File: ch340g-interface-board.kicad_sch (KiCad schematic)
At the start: 10 parts, among them J1 61729-1011BLF, J2 Conn_01x02_Pin, J3 Conn_01x06_Pin, U1 CH340G, Y1 12Mhz

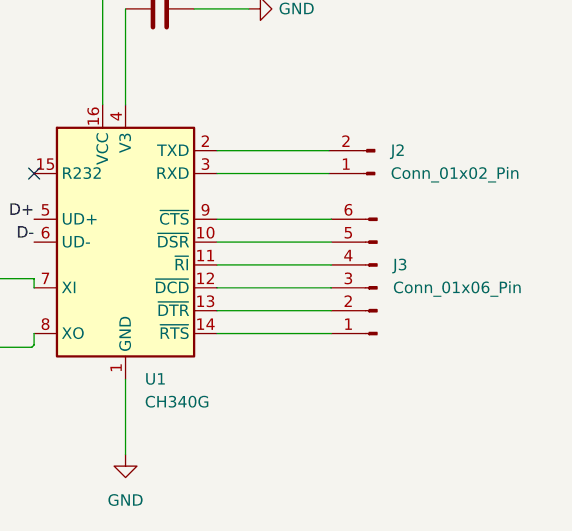
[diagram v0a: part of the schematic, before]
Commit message: documentation: board updates
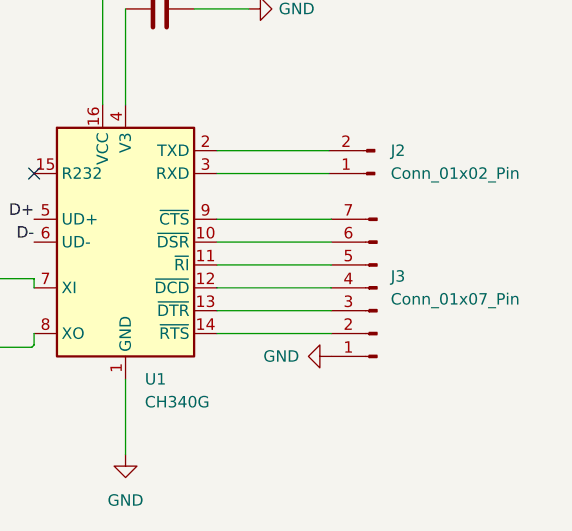
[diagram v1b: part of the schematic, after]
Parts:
- removed J3: Conn_01x06_Pin, Connector_PinHeader_1.00mm:PinHeader_1x06_P1.00mm_Vertical, symbol Connector:Conn_01x06_Pin
- added J3: Conn_01x07_Pin, Connector_PinHeader_1.00mm:PinHeader_1x07_P1.00mm_Vertical, symbol Connector:Conn_01x07_Pin
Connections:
- net GND: now also J3.1 (Pin_1)
- net at U1.10 (~{DSR}): now also J3.6 (Pin_6)
- net at U1.11 (~{RI}): now also J3.5 (Pin_5)
- net at U1.12 (~{DCD}): now also J3.4 (Pin_4)
- net at U1.13 (~{DTR}): now also J3.3 (Pin_3)
- net at U1.14 (~{RTS}): now also J3.2 (Pin_2)
- net at U1.9 (~{CTS}): now also J3.7 (Pin_7)
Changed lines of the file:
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@@
-	)
-	(symbol
-		(lib_id "Connector:Conn_01x06_Pin")
-		(at 136.906 63.5 180)
-		(unit 1)
-		(exclude_from_sim no)
-		(in_bom yes)
-		(on_board yes)
-		(dnp no)
-		(fields_autoplaced yes)
-		(property "Reference" "J3"
-			(at 138.684 60.9599 0)
-			(effects
-				(font
-					(size 1.27 1.27)
-				)
-				(justify right)
-			)
-		)
-		(property "Value" "Conn_01x06_Pin"
-			(at 138.684 63.4999 0)
-			(effects
-				(font
-					(size 1.27 1.27)
-				)
-				(justify right)
-			)
-		)
-		(property "Footprint" "Connector_PinHeader_1.00mm:PinHeader_1x06_P1.00mm_Vertical"
-			(at 136.906 63.5 0)
-			(effects
-				(font
-					(size 1.27 1.27)
-				)
-				(hide yes)
-			)
-		)
-		(property "Datasheet" "~"
-			(at 136.906 63.5 0)
-			(effects
-				(font
-					(size 1.27 1.27)
-				)
-				(hide yes)
-			)
-		)
-		(property "Description" "Generic connector, single row, 01x06, script generated"
-			(at 136.906 63.5 0)
-			(effects
-				(font
-					(size 1.27 1.27)
-				)
-				(hide yes)
-			)
-		)
-		(pin "4"
-		)
-		(pin "5"
-		)
-		(pin "6"
-		)
-		(pin "1"
-		)
-		(pin "2"
-		)
-		(pin "3"
-		)
-		(instances
-			(project ""
-				(path "/1242ce71-0b74-4298-a9a8-725f79ae9887"
-					(reference "J3")
-					(unit 1)
-				)
-			)
-		)
 	)
 	(symbol
@@
 	)
 	(symbol
+		(lib_id "Connector:Conn_01x07_Pin")
+		(at 136.906 63.5 180)
+		(unit 1)
+		(exclude_from_sim no)
+		(in_bom yes)
+		(on_board yes)
+		(dnp no)
+		(fields_autoplaced yes)
+		(property "Reference" "J3"
+			(at 138.43 62.2299 0)
+			(effects
+				(font
+					(size 1.27 1.27)
+				)
+				(justify right)
+			)
+		)
+		(property "Value" "Conn_01x07_Pin"
+			(at 138.43 64.7699 0)
+			(effects
+				(font
+					(size 1.27 1.27)
+				)
+				(justify right)
+			)
+		)
+		(property "Footprint" "Connector_PinHeader_1.00mm:PinHeader_1x07_P1.00mm_Vertical"
+			(at 136.906 63.5 0)
+			(effects
+				(font
+					(size 1.27 1.27)
+				)
+				(hide yes)
+			)
+		)
+		(property "Datasheet" "~"
+			(at 136.906 63.5 0)
+			(effects
+				(font
+					(size 1.27 1.27)
+				)
+				(hide yes)
+			)
+		)
+		(property "Description" "Generic connector, single row, 01x07, script generated"
+			(at 136.906 63.5 0)
+			(effects
+				(font
+					(size 1.27 1.27)
+				)
+				(hide yes)
+			)
+		)
+		(pin "2"
+		)
+		(pin "1"
+		)
+		(pin "3"
+		)
+		(pin "4"
+		)
+		(pin "5"
+		)
+		(pin "6"
+		)
+		(pin "7"
+		)
+		(instances
+			(project ""
+				(path "/1242ce71-0b74-4298-a9a8-725f79ae9887"
+					(reference "J3")
+					(unit 1)
+				)
+			)
+		)
+	)
+	(symbol
 		(lib_id "Device:C")
 		(at 73.66 75.692 90)
@@
 					(unit 1)
 				)
+			)
+		)
+	)
+	(symbol
+		(lib_id "power:GND")
+		(at 131.826 71.12 270)
+		(unit 1)
+		(exclude_from_sim no)
+		(in_bom yes)
+		(on_board yes)
+		(dnp no)
+		(fields_autoplaced yes)
+		(property "Reference" "#PWR07"
+			(at 125.476 71.12 0)
+			(effects
+				(font
+					(size 1.27 1.27)
+				)
+				(hide yes)
+			)
+		)
+		(property "Value" "GND"
+			(at 128.27 71.1199 90)
+			(effects
+				(font
+					(size 1.27 1.27)
+				)
+				(justify right)
+			)
+		)
+		(property "Footprint" ""
+			(at 131.826 71.12 0)
+			(effects
+				(font
+					(size 1.27 1.27)
+				)
+				(hide yes)
+			)
+		)
+		(property "Datasheet" ""
+			(at 131.826 71.12 0)
+			(effects
+				(font
+					(size 1.27 1.27)
+				)
+				(hide yes)
+			)
+		)
+		(property "Description" "Power symbol creates a global label with name \"GND\" , ground"
+			(at 131.826 71.12 0)
+			(effects
+				(font
+					(size 1.27 1.27)
+				)
+				(hide yes)
+			)
+		)
+		(pin "1"
+		)
+		(instances
+			(project ""
+				(path "/1242ce71-0b74-4298-a9a8-725f79ae9887"
+					(reference "#PWR07")
+					(unit 1)
+				)

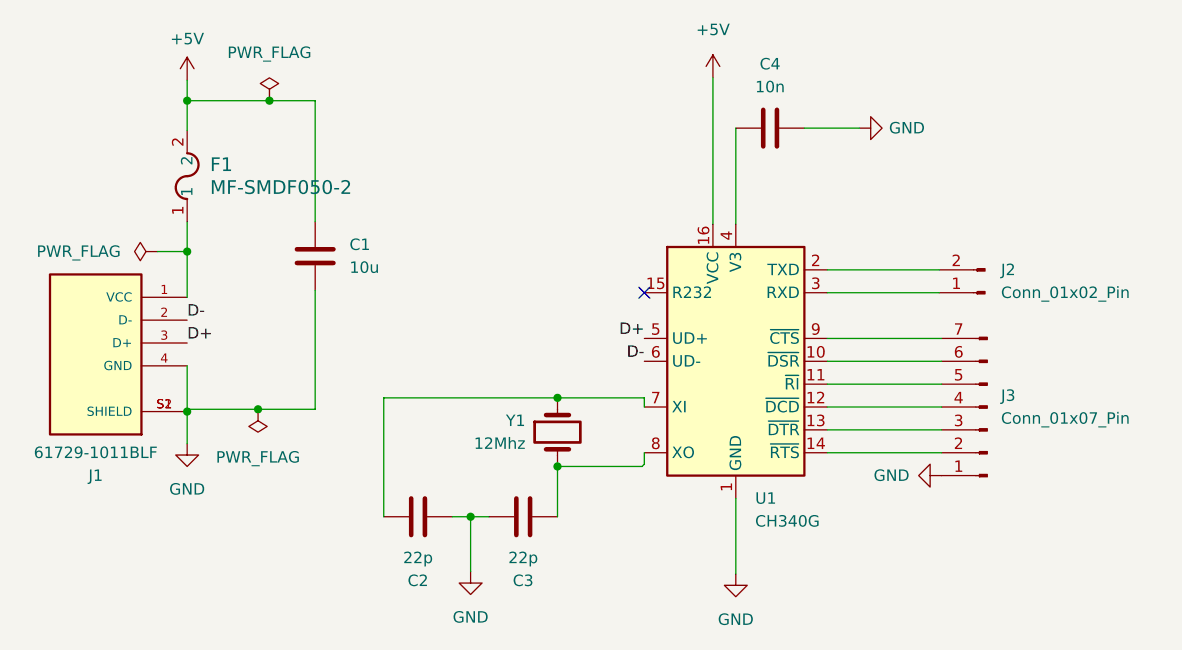
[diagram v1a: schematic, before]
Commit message: documentation: board updates
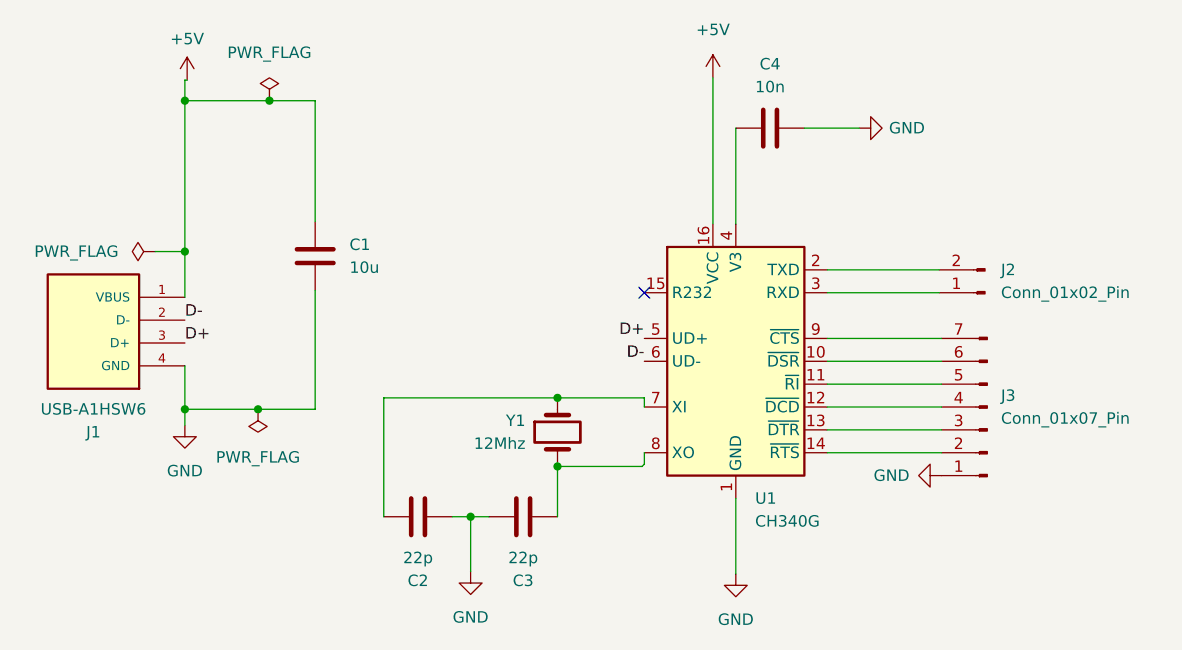
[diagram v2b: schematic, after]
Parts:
- removed F1: MF-SMDF050-2, FUSE_SMDF050-2:FUSE_SMDF050-2, symbol MF-SMDF050-2:MF-SMDF050-2
- removed J1: 61729-1011BLF, 61729-1011BLF:AMPHENOL_61729-1011BLF, symbol 61729-1011BLF:61729-1011BLF
- added J1: USB-A1HSW6, USB-A1HSW6:OST_USB-A1HSW6, symbol USB-A1HSW6:USB-A1HSW6
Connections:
- net +5V: now also J1.1 (VBUS)
- net D+: now also J1.3 (D+)
- net D-: now also J1.2 (D-)
- net GND: now also J1.4 (GND)
